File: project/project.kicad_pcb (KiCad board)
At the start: 2 copper layers, 40 x 65 mm, 55 parts, among them J1 ssd1306 oled, Q1 AO3401A, SW1 USR_BTN, SW2 USR_BTN, T1 PJ-242, T2 PJ-242, T3 PJ-242, T4 PJ-242, T5 PJ-242, T6 PJ-242, T7 PJ-242, T8 PJ-242, U1 esp32-c3-supermini

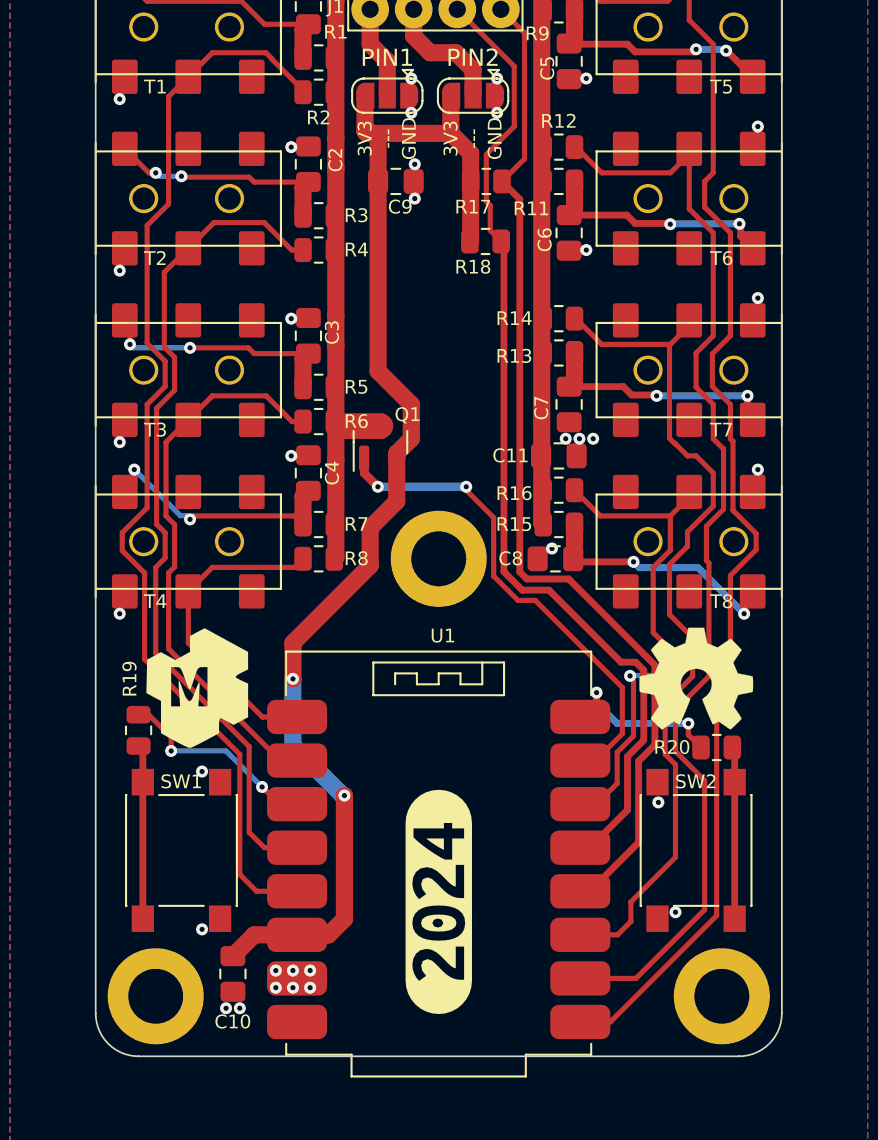
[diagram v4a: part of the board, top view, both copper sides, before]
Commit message: numbering inputs, changing buttons, and adding tooling holes
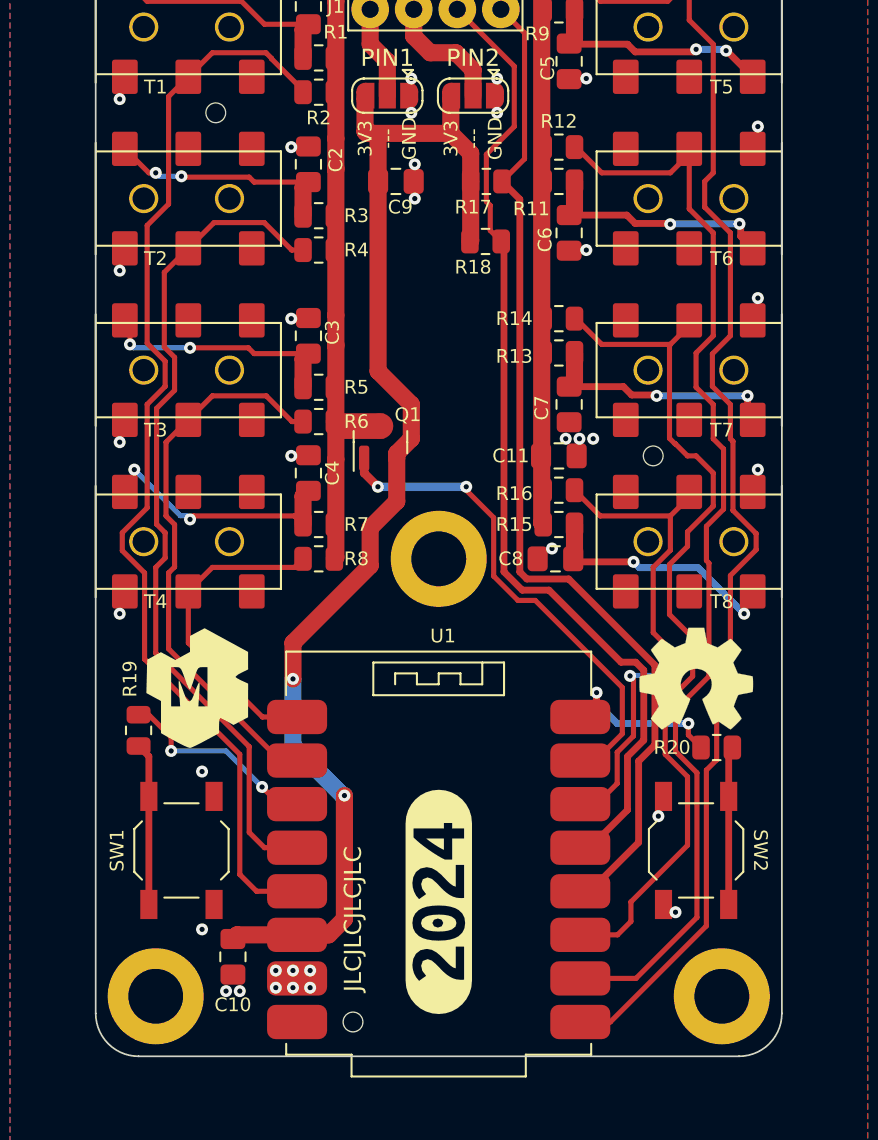
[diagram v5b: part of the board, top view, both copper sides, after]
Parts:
- removed kibuzzard-674CCC3B: G***, kibuzzard-674CCC3B
- added REF**: toolhole, -local:toolhole, F.Cu at (134.3, 77.0)
- added REF**: toolhole, -local:toolhole, F.Cu at (142.3, 130.0)
- added REF**: toolhole, -local:toolhole, F.Cu at (159.8, 97.0)
- added kibuzzard-6769ABD9: G***, kibuzzard-6769ABD9, B.Cu at (164.5, 114.0)
- added kibuzzard-6769ACE8: G***, kibuzzard-6769ACE8, B.Cu at (132.8, 72.0)
- added kibuzzard-6769ACFC: G***, kibuzzard-6769ACFC, B.Cu at (161.8, 72.0)
- added kibuzzard-6769AD03: G***, kibuzzard-6769AD03, B.Cu at (161.8, 82.0)
- added kibuzzard-6769AD0A: G***, kibuzzard-6769AD0A, B.Cu at (161.8, 92.0)
- added kibuzzard-6769AD10: G***, kibuzzard-6769AD10, B.Cu at (161.8, 102.0)
- added kibuzzard-6769AD24: G***, kibuzzard-6769AD24, B.Cu at (132.8, 82.0)
- added kibuzzard-6769AD2C: G***, kibuzzard-6769AD2C, B.Cu at (132.8, 92.0)
- added kibuzzard-6769B10C: G***, kibuzzard-6769B10C, B.Cu at (132.8, 102.0)
- SW1, SW2: footprint Button_Switch_SMD:SW_SPST_PTS645 -> Button_Switch_SMD:SW_SPST_TL3342
- moved C10 1.00 mm to (135.3, 126.2)
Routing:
- net Net-(R20-Pad2): track 10.0 -> 9.24 mm
- net Net-(R19-Pad2): track 10.2 -> 9.49 mm
- net T7: track 50.0 -> 50.5 mm
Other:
- board text added: "JLCJLCJLCJLC"
- board text added: "http://temp-1w8-pro.makerspace.lt/v3.1"
- board text removed: "http://temp-1w8-pro.makerspace.lt/v3.0"

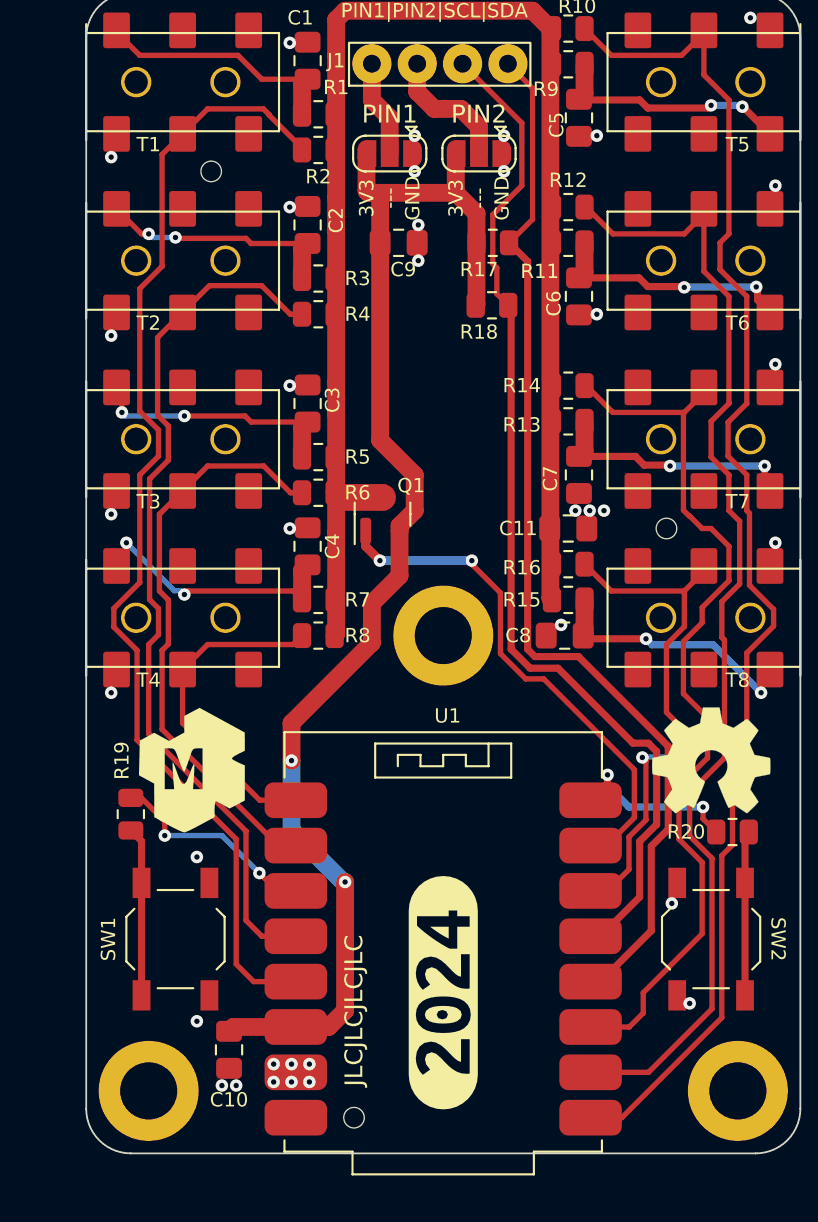
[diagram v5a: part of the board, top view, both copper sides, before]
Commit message: replacing power fet with resistor
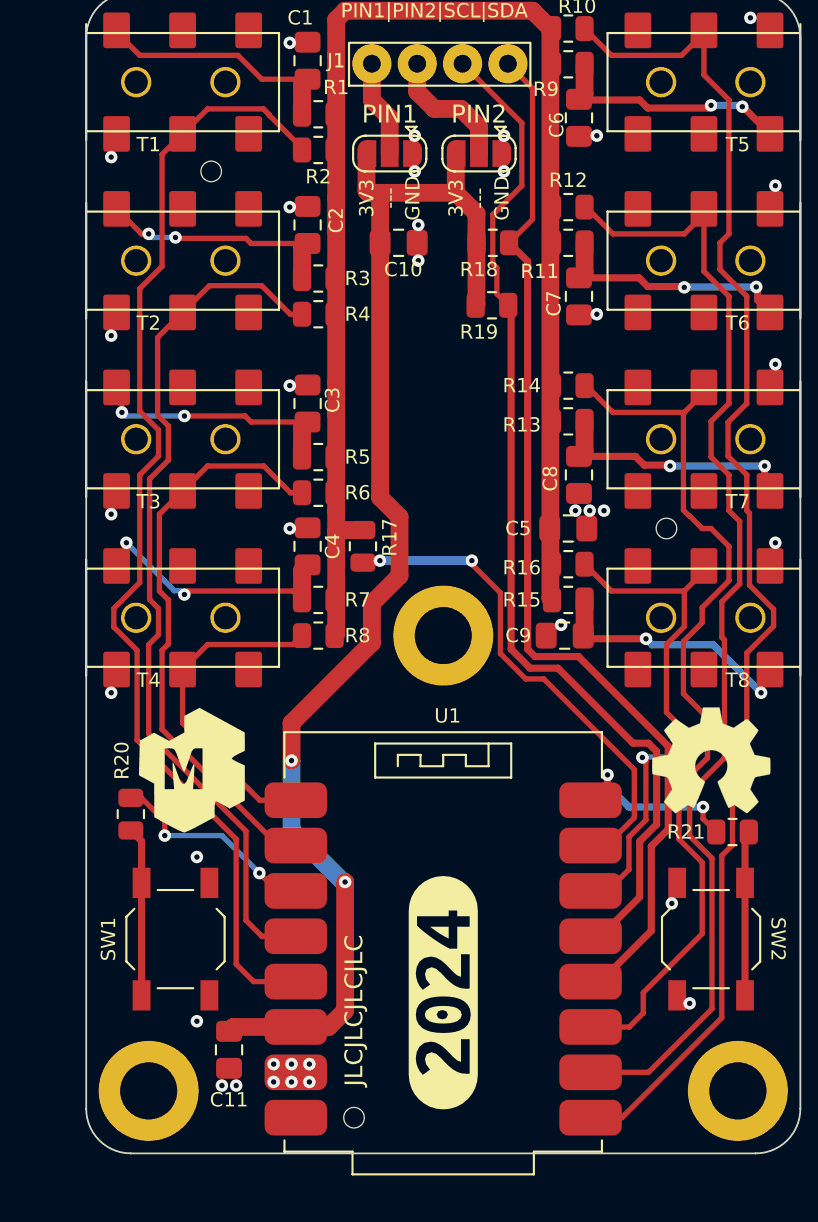
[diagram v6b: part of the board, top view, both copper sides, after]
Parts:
- removed Q1: AO3401A, Package_TO_SOT_SMD:SOT-23
- removed kibuzzard-6769ABD9: G***, kibuzzard-6769ABD9
- added R17: 100, Resistor_SMD:R_0805_2012Metric, F.Cu at (142.8, 98.0)
- added kibuzzard-6771C807: G***, kibuzzard-6771C807, B.Cu at (164.5, 114.0)
- renumbered C9 to C10, C10 to C11, C11 to C5, C5 to C6, C6 to C7, C7 to C8, C8 to C9, R17 to R18, R18 to R19, R19 to R20, R20 to R21
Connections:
- U1 pad 7: 1W_NRST -> 1W_PWR
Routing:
- net 1W_NRST: track 29.0 -> 0.00 mm, vias 2 -> 0
- net 1W_PWR: track 0.00 -> 27.0 mm, vias 0 -> 2
- net /_TVCC: track 82.2 -> 81.0 mm
- net +3V3: track 74.0 -> 73.3 mm
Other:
- board text added: "http://temp-1w8-pro.makerspace.lt/v4.0"
- board text removed: "http://temp-1w8-pro.makerspace.lt/v3.1"
